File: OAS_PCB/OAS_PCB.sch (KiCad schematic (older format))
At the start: 19 parts

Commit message: Increased schematic sheet size, added+/- voltage regulators
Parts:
- added U?: LM337_TO220, Package_TO_SOT_THT:TO-220-3_Vertical, symbol Regulator_Linear:LM337_TO220
- added U?: LM317_TO-220, Package_TO_SOT_THT:TO-220-3_Vertical, symbol Regulator_Linear:LM317_TO-220
- added U?: CD4051B, symbol Analog_Switch:CD4051B
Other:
- moved on the sheet: AS?, D1, D2, D3, D4, DAC?, Rt, U?

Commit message: added power terminal block and -6.5 V negative voltage supply
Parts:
- added C? (x2): 1µF, symbol Device:CP1
- added J?: Screw_Terminal_01x04, symbol Connector:Screw_Terminal_01x04
- added R?: 120Ω, symbol Device:R
- added R?: 525Ω, symbol Device:R
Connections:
- net GND: now also C?.1, C?.1, J?.3 (Pin_3), R?.1
- net at U?.1 (ADJ): now also R?.1, R?.2
- net -12: now reaches U?.2 (VI)
- net -12: now also C?.2, J?.4 (Pin_4)
- net -6.5: now reaches U?.3 (VO)
- net -6.5: now also C?.2, R?.2
- net +12: now reaches U?.3 (VI)
- net +12: now also J?.1 (Pin_1)
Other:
- note added: "Power_input"
- note added: "V+"
- note added: "V-"
- moved on the sheet: AS?, D1, D2, D3, D4, Rt, U?

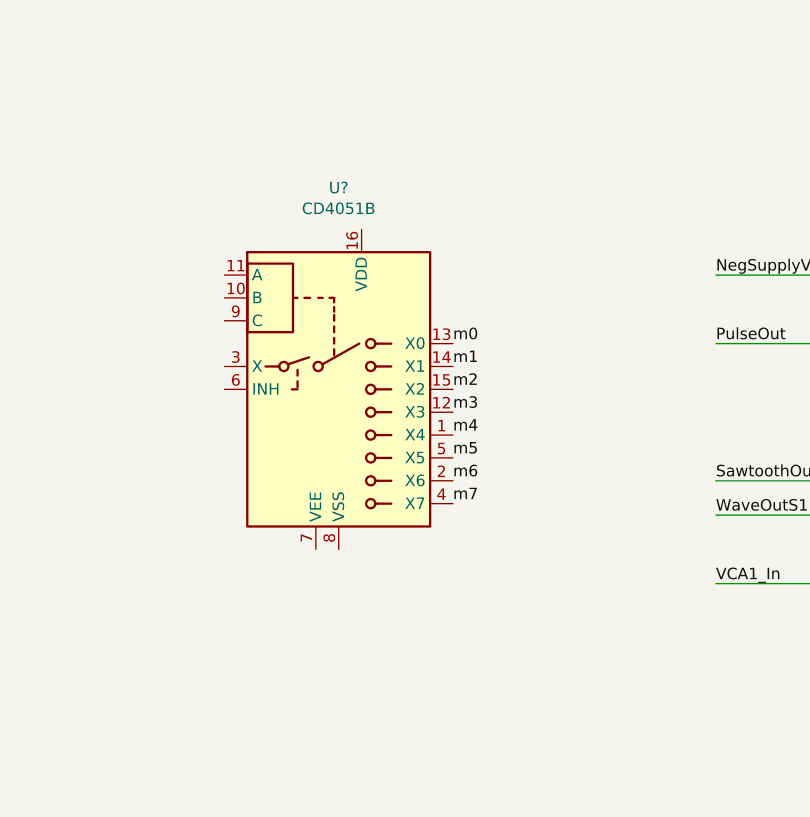
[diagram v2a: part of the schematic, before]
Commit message: Added each individual hold capacitor to the first MUX chip. Can be duplicated now easily. Added labels to correlate to specific CVs on the AS chip.
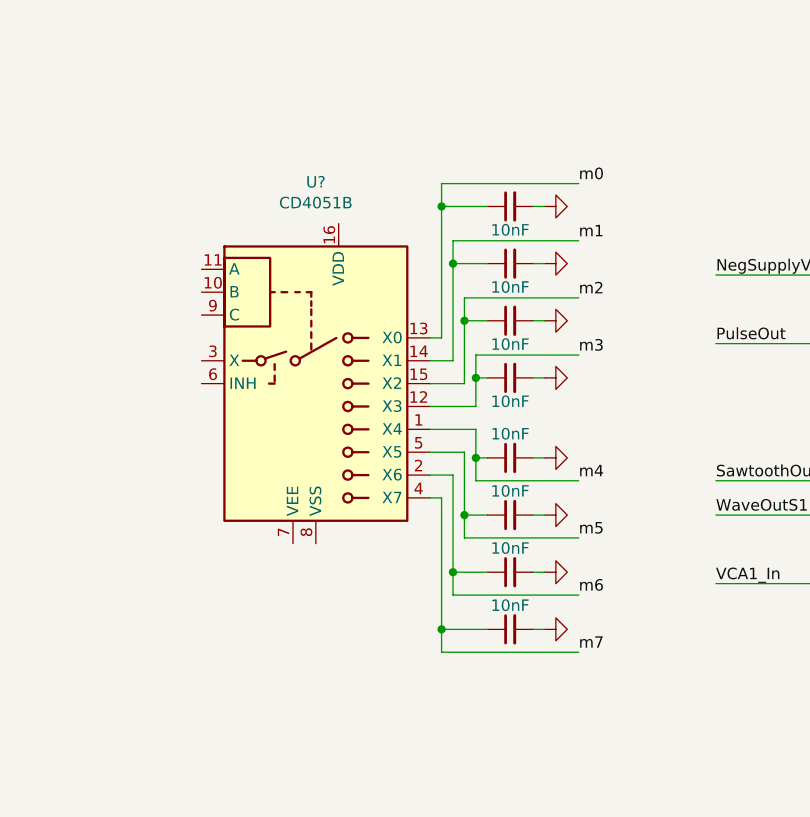
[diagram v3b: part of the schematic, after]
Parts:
- added Ct? (x8): 10nF, symbol Device:C_Small
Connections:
- net GND: now also Ct?.2, Ct?.2, Ct?.2, Ct?.2, Ct?.2, Ct?.2, Ct?.2, Ct?.2
- net m0: now also Ct?.1
- net m1: now also Ct?.1
- net m2: now also Ct?.1
- net m3: now also Ct?.1
- net m4: now also Ct?.1
- net m5: now also Ct?.1
- net m6: now also Ct?.1
- net m7: now also Ct?.1
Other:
- moved on the sheet: U?

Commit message: finished AS3394 power supply and connected wave_out to VCA1_in
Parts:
- removed C? (x2): 1µF, symbol Device:CP1
- removed J?: Screw_Terminal_01x04, symbol Connector:Screw_Terminal_01x04
- removed R?: 120Ω, symbol Device:R
- removed R?: 525Ω, symbol Device:R
- removed U?: LM337_TO220, Package_TO_SOT_THT:TO-220-3_Vertical, symbol Regulator_Linear:LM337_TO220
- removed U?: LM317_TO-220, Package_TO_SOT_THT:TO-220-3_Vertical, symbol Regulator_Linear:LM317_TO-220
- added C? (x2): 1 µ, symbol Device:CP1_Small
- added C? (x2): 10 µ, symbol Device:CP1_Small
- added C? (x2): .1µ, symbol Device:C
- added D? (x4): 1N4002, Diode_THT:D_DO-41_SOD81_P10.16mm_Horizontal, symbol Diode:1N4002
- added J?: Screw_Terminal_01x04, symbol Connector:Screw_Terminal_01x04
- added R? (x2): 120, symbol Device:R
- added R?: 525, symbol Device:R
- added R?: 360, symbol Device:R
- added U?: LM337_TO220, Package_TO_SOT_THT:TO-220-3_Vertical, symbol Regulator_Linear:LM337_TO220
- added U?: LM317_TO-220, Package_TO_SOT_THT:TO-220-3_Vertical, symbol Regulator_Linear:LM317_TO-220
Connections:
- net WaveOutS1 is gone; now on net VCA1_In: AS?.10 (Wave_Out), AS?.11 (VCA1), R?.1, R?.1
- net +12: now also C?.1, D?.1 (K), J?.1 (Pin_1), U?.3 (VI)
- net -12: now also C?.2, D?.2 (A), J?.4 (Pin_4), U?.2 (VI)
- net GND: now also C?.1, C?.1, C?.1, C?.2, C?.2, C?.2, J?.3 (Pin_3), R?.1, R?.2
- net NegSupplyVin renamed -6.5V
- net -6.5V: now also C?.2, D?.1 (K), D?.2 (A), R?.2, U?.3 (VO)
- net PosSupplyVin renamed +5V
- net +5V: now also C?.1, D?.1 (K), D?.2 (A), R?.1, U?.2 (VO)
- new net: C?.2, D?.1 (K), R?.1, R?.2, U?.1 (ADJ)
- new net: C?.1, D?.2 (A), R?.1, R?.2, U?.1 (ADJ)
- new net +5MCU: J?.2 (Pin_2)
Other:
- note removed: "V+"
- note removed: "V-"
- moved on the sheet: DAC?

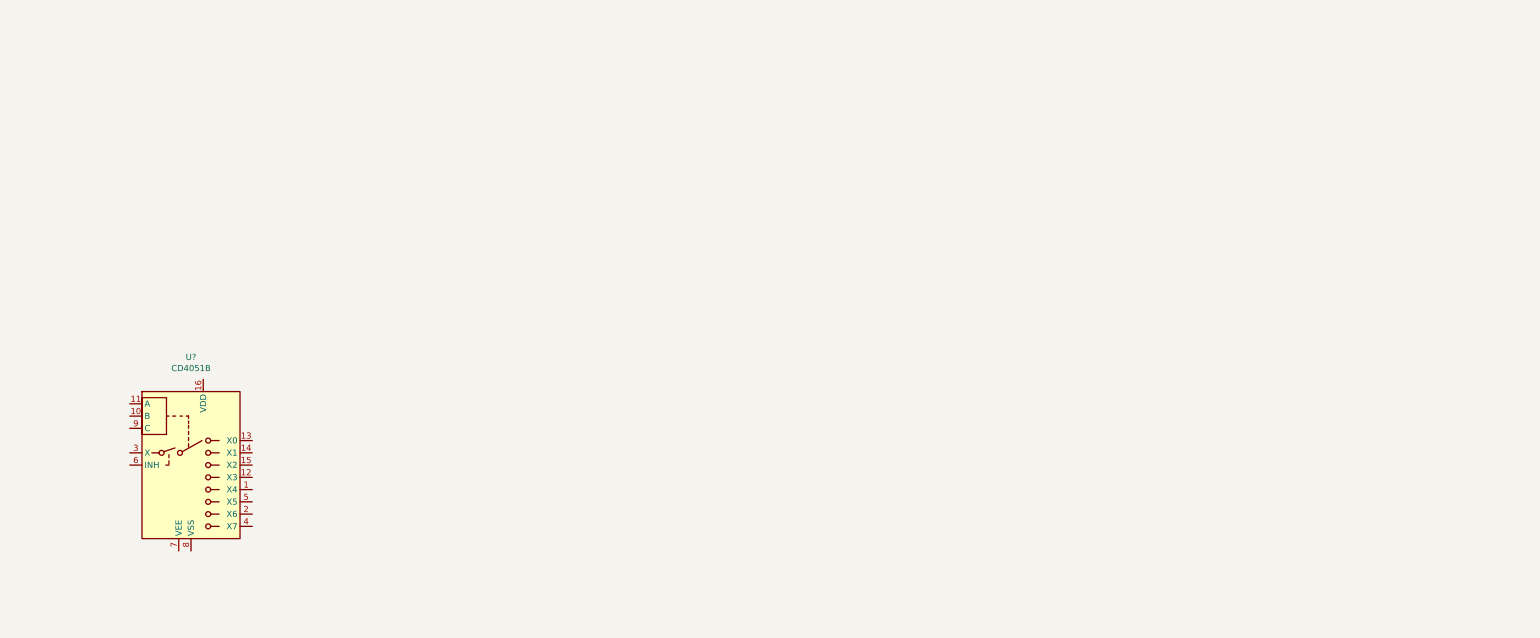
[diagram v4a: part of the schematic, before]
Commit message: Added Teensy symbol and footprint. Linked footprints for AS3394 and Teensy.
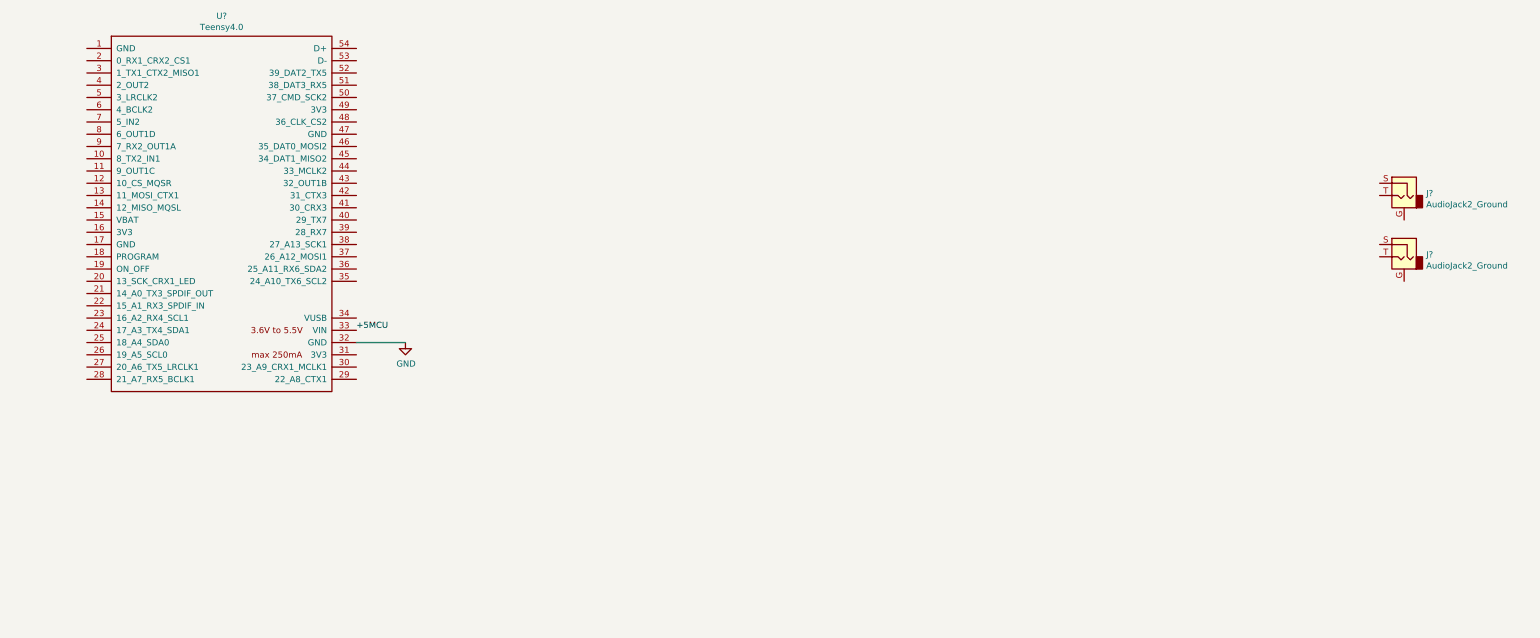
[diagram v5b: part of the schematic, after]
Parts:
- removed U?: CD4051B, symbol Analog_Switch:CD4051B
- added J? (x2): AudioJack2_Ground, symbol Connector:AudioJack2_Ground
- added U?: Teensy4.0, teensy:Teensy40, symbol teensy:Teensy4.0
- AS?: footprint (none) -> Package_SO:SOIC-24W_7.5x15.4mm_P1.27mm
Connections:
- net +5MCU: now also U?.33 (VIN)
- net GND: now also U?.32 (GND)
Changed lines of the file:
@@
 F 0 "AS?" H 15950 14175 50  0000 C CNN
 F 1 "AS3394" H 15950 14084 50  0000 C CNN
-F 2 "" H 16000 13500 50  0001 C CNN
+F 2 "Package_SO:SOIC-24W_7.5x15.4mm_P1.27mm" H 16000 13500 50  0001 C CNN
 F 3 "" H 16000 13500 50  0001 C CNN
 	1    15950 13300
@@
 F 3 "http://www.ti.com/lit/ds/symlink/cd4052b.pdf" H 12380 13525 50  0001 C CNN
 	1    12400 13425
-	1    0    0    -1
-$EndComp
-$Comp
-L Analog_Switch:CD4051B U?
-U 1 1 601D6AD7
-P 10500 9650
-F 0 "U?" H 10500 10531 50  0000 C CNN
-F 1 "CD4051B" H 10500 10440 50  0000 C CNN
-F 2 "" H 10650 8900 50  0001 L CNN
-F 3 "http://www.ti.com/lit/ds/symlink/cd4052b.pdf" H 10480 9750 50  0001 C CNN
-	1    10500 9650
 	1    0    0    -1
 $EndComp
@@
 	14800 12950 14400 12950
 Connection ~ 14800 12950
+$Comp
+L Connector:AudioJack2_Ground J?
+U 1 1 602102C1
+P 20400 7450
+F 0 "J?" H 20220 7468 50  0000 R CNN
+F 1 "AudioJack2_Ground" H 20220 7377 50  0000 R CNN
+F 2 "" H 20400 7450 50  0001 C CNN
+F 3 "~" H 20400 7450 50  0001 C CNN
+	1    20400 7450
+	-1   0    0    -1
+$EndComp
+$Comp
+L Connector:AudioJack2_Ground J?
+U 1 1 602145F4
+P 20400 7950
+F 0 "J?" H 20220 7968 50  0000 R CNN
+F 1 "AudioJack2_Ground" H 20220 7877 50  0000 R CNN
+F 2 "" H 20400 7950 50  0001 C CNN
+F 3 "~" H 20400 7950 50  0001 C CNN
+	1    20400 7950
+	-1   0    0    -1
+$EndComp
+$Comp
+L teensy:Teensy4.0 U?
+U 1 1 601D3644
+P 10750 7600
+F 0 "U?" H 10750 9215 50  0000 C CNN
+F 1 "Teensy4.0" H 10750 9124 50  0000 C CNN
+F 2 "teensy:Teensy40" H 10350 7800 50  0001 C CNN
+F 3 "" H 10350 7800 50  0001 C CNN
+	1    10750 7600
+	1    0    0    -1
+$EndComp
+Text Label 11850 8550 0    50   ~ 0
++5MCU
+$Comp
+L power:GND #PWR?
+U 1 1 601D6CDD
+P 12250 8650
+F 0 "#PWR?" H 12250 8400 50  0001 C CNN
+F 1 "GND" H 12255 8477 50  0000 C CNN
+F 2 "" H 12250 8650 50  0001 C CNN
+F 3 "" H 12250 8650 50  0001 C CNN
+	1    12250 8650
+	1    0    0    -1
+$EndComp
+Wire Wire Line
+	11850 8650 12250 8650
 $EndSCHEMATC
